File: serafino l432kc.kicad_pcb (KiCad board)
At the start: 4 copper layers, 31 parts, among them J1 USB_B_Micro, J2 Conn_01x14, J3 Conn_01x14, Q1 AO3401A, SW1 SW_Push, SW2 SW_Push, U1 AP2112K-3.3, U2 USBLC6-2SC6, U3 STM32L432KCUx, Y1 32.768K

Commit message: Nuevo layout
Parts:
- moved SW2 65.1 mm to (198.1, 124.2)
- moved C10 58.7 mm to (200.4, 115.8)
- moved D4 56.9 mm to (191.8, 126.2), turned to 270 degrees
- moved C9 56.3 mm to (200.4, 118.9)
- moved L1 54.7 mm to (200.4, 117.3), turned to 180 degrees
- moved R4 52.8 mm to (193.3, 126.2), turned to 270 degrees
- moved R3 52.5 mm to (193.3, 123.2), turned to 270 degrees
- moved C8 52.3 mm to (201.4, 107.2), turned to 90 degrees
- moved R1 52.3 mm to (193.3, 120.1), turned to 270 degrees
- moved D1 52.2 mm to (191.8, 120.2), turned to 270 degrees
- moved D3 52.2 mm to (191.8, 123.2), turned to 270 degrees
- moved C6 46.5 mm to (199.6, 107.2)
- moved C7 46.4 mm to (194.6, 114.3), turned to 180 degrees
- moved C1 46.1 mm to (192.5, 105.4), turned to 270 degrees
- moved R2 45.5 mm to (192.8, 114.5), turned to 90 degrees
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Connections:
- J2 pad 5: SWCLK -> SWDIO
- J2 pad 6: SWDIO -> SWCLK
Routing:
- net BOOT0: track 0.00 -> 14.8 mm
- net SWDIO: track 0.00 -> 10.2 mm, vias 0 -> 1
- net USART2_RX: track 0.00 -> 9.19 mm
- net PB5: track 0.00 -> 9.14 mm
- net LED0: track 0.00 -> 8.78 mm
- net PB4: track 0.00 -> 8.07 mm
- net SWCLK: track 0.00 -> 8.01 mm, vias 0 -> 1
- net NRST: track 0.00 -> 7.72 mm, vias 0 -> 1
- net SAI1_FS_B: track 0.00 -> 7.18 mm
- net SPI1_SS: track 0.00 -> 7.12 mm
- net BTN0: track 0.00 -> 6.74 mm, vias 0 -> 1
- net SAI1_SCK_B: track 0.00 -> 6.67 mm
- net LED2: track 0.00 -> 5.38 mm
- net I2C1_SDA: track 0.00 -> 5.23 mm, vias 0 -> 1
- net SPI1_MOSI: track 0.00 -> 5.16 mm
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
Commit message: new layout
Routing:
- net BOOT0: track 14.8 -> 0.00 mm
- net SWDIO: track 10.2 -> 0.00 mm, vias 1 -> 0
- net USART2_RX: track 9.19 -> 0.00 mm
- net PB5: track 9.14 -> 0.00 mm
- net LED0: track 8.78 -> 0.00 mm
- net PB4: track 8.07 -> 0.00 mm
- net SWCLK: track 8.01 -> 0.00 mm, vias 1 -> 0
- net NRST: track 7.72 -> 0.00 mm, vias 1 -> 0
- net USB_D-: track 7.69 -> 0.00 mm
- net SAI1_FS_B: track 7.18 -> 0.00 mm
- net SPI1_SS: track 7.12 -> 0.00 mm
- net USB_D+: track 6.83 -> 0.00 mm
- net BTN0: track 6.74 -> 0.00 mm, vias 1 -> 0
- net SAI1_SCK_B: track 6.67 -> 0.00 mm
- net LED2: track 5.38 -> 0.00 mm
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
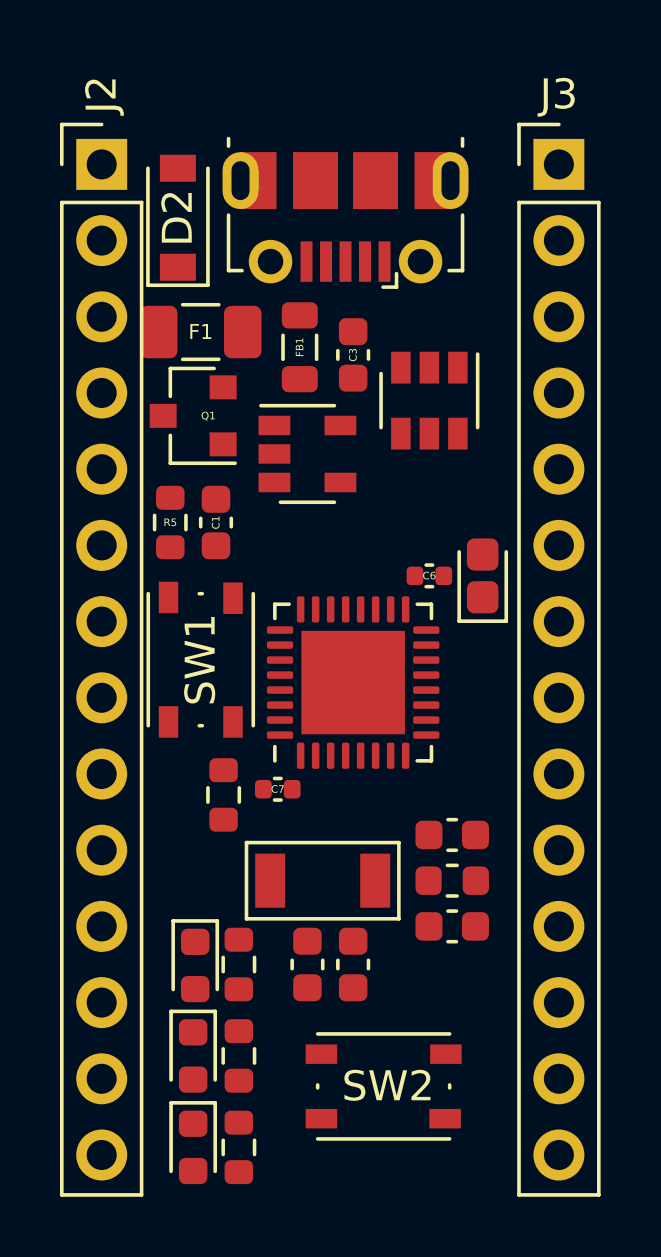
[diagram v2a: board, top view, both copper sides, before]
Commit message: removed user button
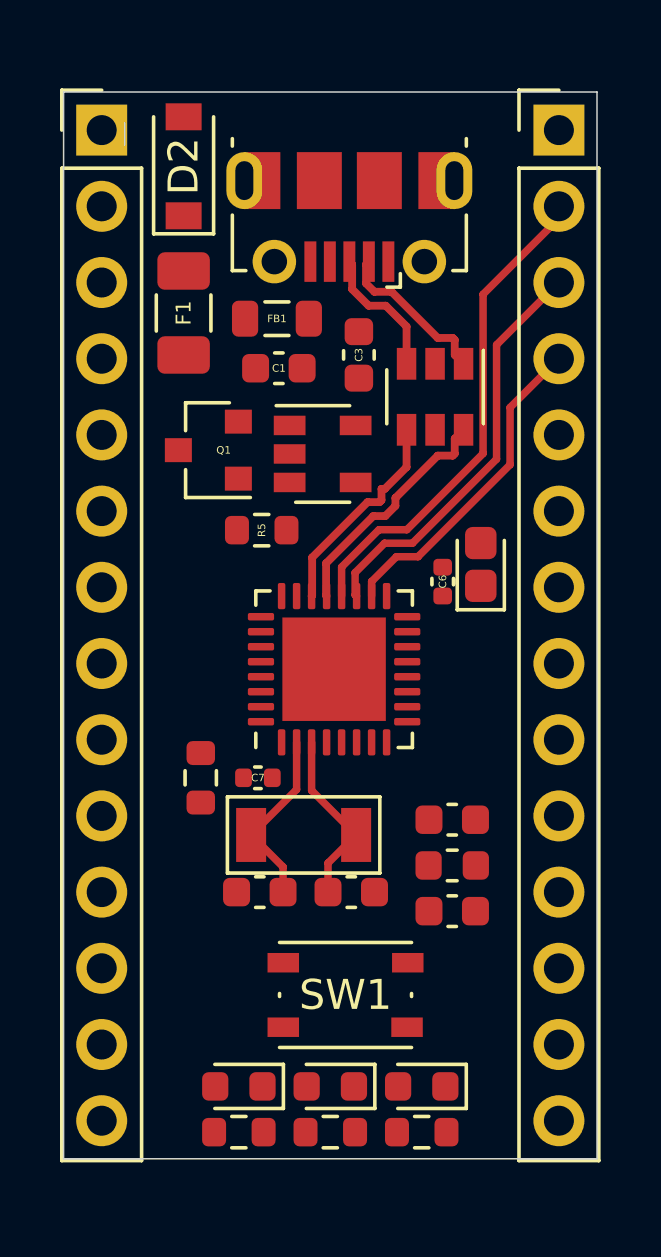
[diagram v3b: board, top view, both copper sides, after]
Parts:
- removed SW2: SW_Push, Button_Switch_SMD:SW_Push_1P1T_NO_Vertical_Wuerth_434133025816
- moved SW1 12.2 mm to (196.8, 121.2), turned to 0 degrees
- moved D1 8.56 mm to (199.4, 124.2), turned to 180 degrees
- moved R1 8.27 mm to (199.4, 125.7), turned to 180 degrees
- moved C1 5.55 mm to (194.6, 100.3), turned to 180 degrees
- moved D3 4.68 mm to (196.3, 124.2), turned to 180 degrees
- moved R3 3.97 mm to (196.3, 125.7), turned to 180 degrees
- moved R5 3.06 mm to (194.1, 105.7), turned to 180 degrees
- moved C4 2.89 mm to (194.0, 117.7), turned to 180 degrees
- moved D4 2.54 mm to (193.3, 124.2), turned to 180 degrees
- moved C5 2.41 mm to (197.0, 117.7), turned to 0 degrees
- moved D2 1.73 mm to (191.5, 93.5)
- moved Y1 1.65 mm to (195.5, 115.8)
- moved Q1 1.25 mm to (192.3, 103.0)
- moved FB1 1.22 mm to (194.6, 98.6), turned to 0 degrees
- moved J2 1.14 mm to (188.7, 92.3)
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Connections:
- net BTN0 renamed PA15
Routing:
- net I2C1_SDA: track 0.00 -> 16.5 mm
- net I2C1_SCL: track 0.00 -> 13.8 mm
- net LED1: track 0.00 -> 10.9 mm
- net USB_D-: track 0.00 -> 7.98 mm
- net USB_D+: track 0.00 -> 7.15 mm
- net HSE_IN: track 0.00 -> 6.06 mm
- net HSE_OUT: track 0.00 -> 6.00 mm
- net USB_CONN_D-: track 0.00 -> 5.42 mm
- net USB_CONN_D+: track 0.00 -> 4.53 mm
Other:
- board outline added: 17.8 x 35.6 mm

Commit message: Tracks...
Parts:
- moved C10 2.55 mm to (200.7, 117.9)
- moved C9 1.05 mm to (200.7, 119.4)
- moved C4 0.64 mm to (194.0, 118.4)
- moved C5 0.64 mm to (197.0, 118.4)
- moved Y1 0.64 mm to (195.5, 116.5)
- moved L1 0.57 mm to (200.7, 116.3)
- moved SW1 0.55 mm to (196.3, 121.3)
- moved C6 0.19 mm to (200.1, 107.6), turned to 270 degrees
- moved C8 0.13 mm to (201.4, 106.9), turned to 270 degrees
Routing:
- net NRST: track 0.00 -> 16.3 mm, vias 0 -> 1
- net PA0: track 0.00 -> 15.6 mm, vias 0 -> 1
- net SPI1_SCK: track 0.00 -> 13.4 mm, vias 0 -> 1
- net USART2_TX: track 0.00 -> 10.6 mm, vias 0 -> 1
- net +3.3VA: track 0.00 -> 5.15 mm
- net +3V3: track 0.00 -> 5.13 mm
- net GND: track 0.00 -> 4.94 mm
- net HSE_OUT: track 6.00 -> 6.63 mm
- net HSE_IN: track 6.06 -> 6.70 mm
- added copper zone on In2.Cu, net +3V3
- added copper zone on In1.Cu, net GND
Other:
- outline, holes or cut-outs redrawn

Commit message: more tracks
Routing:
- net LED1: track 10.9 -> 38.8 mm, vias 0 -> 1
- net LED0: track 0.00 -> 27.4 mm, vias 0 -> 2
- net +5V: track 0.00 -> 23.6 mm, vias 0 -> 2
- net VHIGH: track 0.00 -> 18.5 mm
- net +3V3: track 5.13 -> 22.8 mm, vias 0 -> 2
- net EN: track 0.00 -> 15.6 mm, vias 0 -> 1
- net BOOT0: track 0.00 -> 15.0 mm
- net PB7: track 0.00 -> 12.3 mm
- net Net-(D2-Pad1): track 0.00 -> 10.5 mm, vias 0 -> 2
- net LED2: track 0.00 -> 10.4 mm, vias 0 -> 1
- net PB6: track 0.00 -> 10.3 mm
- net SWDIO: track 0.00 -> 9.41 mm
- net SPI1_SS: track 0.00 -> 8.81 mm
- net PB5: track 0.00 -> 8.55 mm
- net USART2_RX: track 0.00 -> 8.33 mm
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
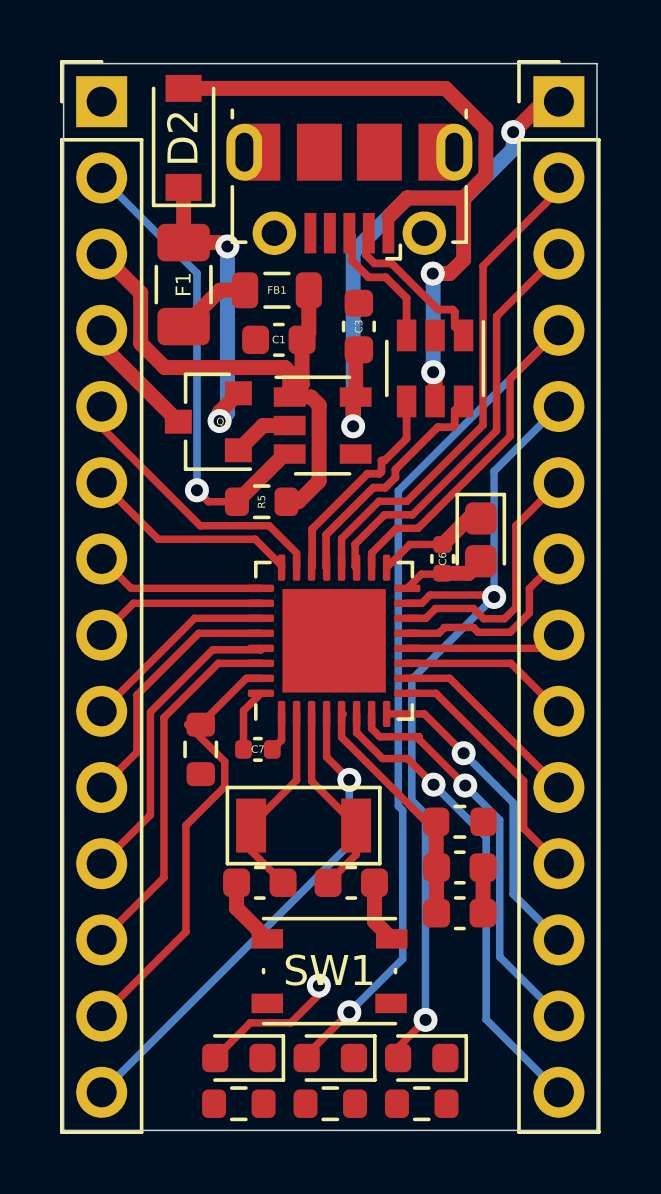
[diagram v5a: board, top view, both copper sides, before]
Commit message: almost finished tracks, 5v is a problem
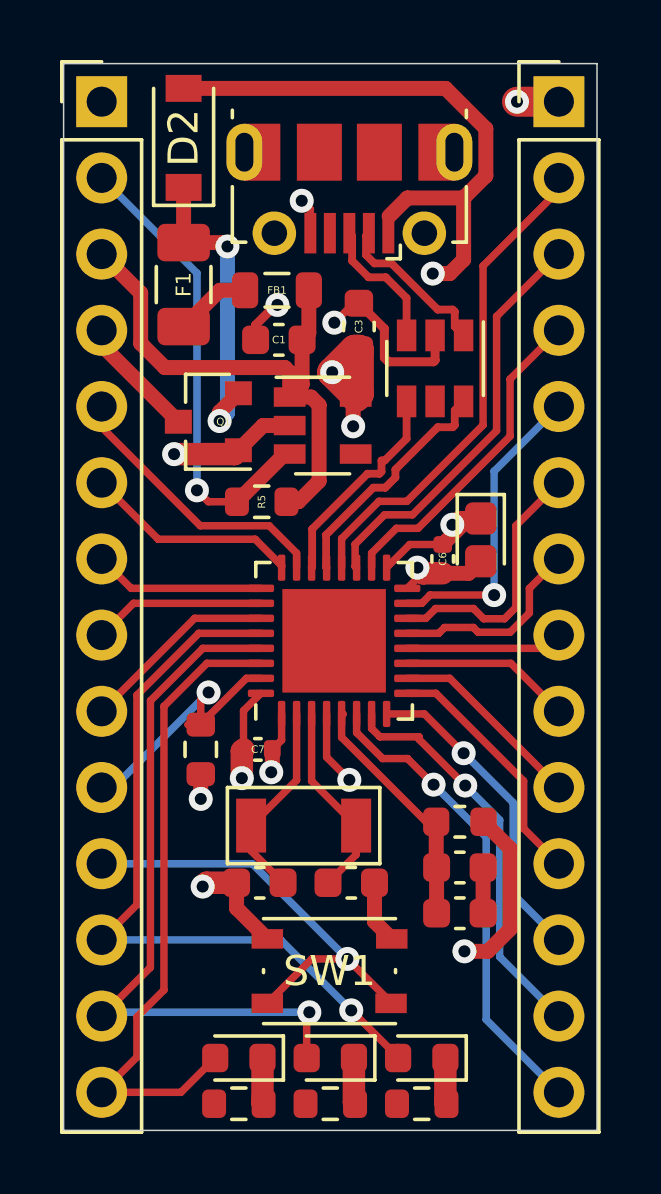
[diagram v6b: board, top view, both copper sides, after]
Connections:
- J2 pad 10: PB5 -> BOOT0
- J2 pad 11: PB6 -> NRST
- J2 pad 12: PB7 -> LED0
- J2 pad 13: BOOT0 -> LED1
- J2 pad 14: NRST -> LED2
- J3 pad 4: LED1 -> PA8
- J3 pad 5: LED0 -> PB1
- J3 pad 9: LED2 -> PA5
- U3 pad 11: LED2 -> PA5
- U3 pad 15: LED0 -> PB1
- U3 pad 18: LED1 -> PA8
- U3 pad 28: PB5 -> LED0
- U3 pad 29: PB6 -> LED1
- U3 pad 30: PB7 -> LED2
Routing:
- net LED1: track 38.8 -> 24.2 mm
- net GND: track 12.9 -> 26.4 mm, vias 0 -> 7
- net PB7: track 12.3 -> 0.00 mm
- net LED2: track 10.4 -> 21.8 mm, vias 1 -> 0
- net PA8: track 0.00 -> 10.9 mm
- net PB6: track 10.3 -> 0.00 mm
- net PB1: track 0.00 -> 10.2 mm, vias 0 -> 1
- net PB5: track 8.55 -> 0.00 mm
- net BOOT0: track 15.0 -> 9.15 mm, vias 0 -> 1
- net PA5: track 0.00 -> 5.72 mm
- net +5V: track 23.6 -> 19.3 mm, vias 2 -> 1
- net +3V3: track 22.8 -> 20.6 mm, vias 2 -> 7
- net LED0: track 27.4 -> 25.5 mm, vias 2 -> 1
- net Net-(D4-Pad1): track 0.00 -> 1.54 mm
- net Net-(D3-Pad1): track 0.00 -> 1.54 mm
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
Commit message: Silk screen
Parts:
- added G***: LOGO, serafino l432kc:logo_materiam, F.Cu at (191.3, 109.5)
- moved R1 1.67 mm to (199.6, 124.1), turned to 0 degrees
- moved R4 1.67 mm to (193.0, 124.1)
- moved R3 1.65 mm to (196.3, 124.1)
- moved D1 1.55 mm to (199.6, 125.7)
- moved D4 1.55 mm to (193.0, 125.7)
- moved D3 1.52 mm to (196.3, 125.7)
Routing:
- net Net-(J1-Pad6): track 0.00 -> 22.4 mm, vias 0 -> 2
- net GND: track 26.4 -> 36.3 mm, vias 7 -> 17
- net NRST: track 17.4 -> 24.9 mm
- net +5V: track 19.3 -> 25.1 mm, vias 1 -> 0
- net +3V3: track 20.6 -> 22.9 mm
- net LED1: track 24.2 -> 26.3 mm
- net LED0: track 25.5 -> 26.8 mm
- net Net-(D1-Pad1): track 1.54 -> 2.32 mm
- net LED2: track 21.8 -> 21.2 mm
- net I2C1_SDA: track 16.5 -> 16.6 mm, vias 0 -> 1
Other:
- board text added: "3.3V"
- board text added: "BOOT0"
- board text added: "EN"
- board text added: "GND"
- board text added: "MISO"
- board text added: "MOSI"
- board text added: "NRST"
- board text added: "PA15"
- board text added: "PA8"
- board text added: "PB1"
- board text added: "PB4"
- board text added: "PB5"
- board text added: "PB6"
- board text added: "PB7"
- board text added: "SAISCK"
- board text added: "SCL"
- board text added: "SDA"
- board text added: "SS"
- board text added: "SWCLK"
- board text added: "SWDIO"
- board text added: "VHIGH"
- board text added: "VIN"

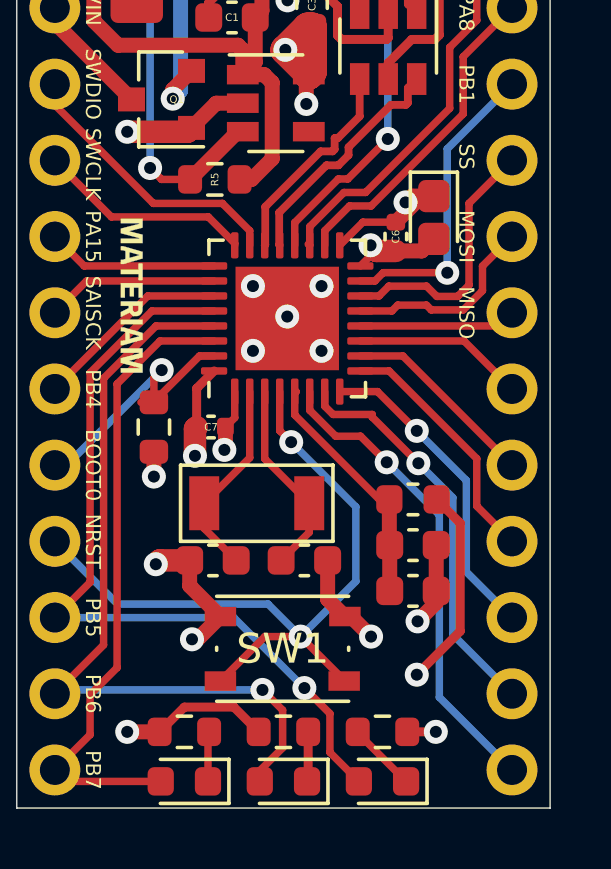
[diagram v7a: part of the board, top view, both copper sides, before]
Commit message: completed tracks
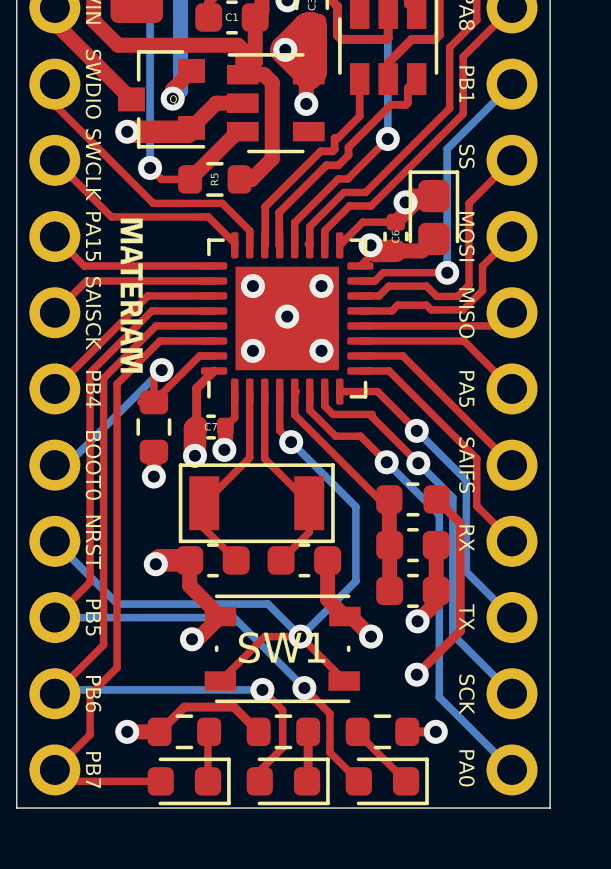
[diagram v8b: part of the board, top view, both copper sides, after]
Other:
- board text added: "PA0"
- board text added: "PA5"
- board text added: "RX"
- board text added: "SAIFS"
- board text added: "SCK"
- board text added: "TX"
